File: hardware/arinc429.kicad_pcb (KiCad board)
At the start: 2 copper layers, 40 x 60 mm, 50 parts, among them P1 CON-SENSOR2, P2 BOOT, P3 DEBUG, P4 IND 8Pol, U1 XMC1404, U2 DRILL, U3 DRILL, U4 DRILL, U5 DRILL, U6 HI-3593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

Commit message: pcb design
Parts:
- moved RP6 43.6 mm to (109.0, 105.9), turned to 180 degrees
- moved D3 42.9 mm to (107.7, 102.6), turned to 270 degrees
- moved D9 41.1 mm to (109.1, 102.6), turned to 270 degrees
- moved D8 39.4 mm to (110.5, 102.6), turned to 270 degrees
- moved C6 21.0 mm to (124.0, 113.1), turned to 90 degrees
- moved P3 19.7 mm to (137.0, 109.2)
- moved C4 19.4 mm to (125.4, 113.1), turned to 90 degrees
- moved P2 17.6 mm to (137.0, 107.3), turned to 180 degrees
- moved C5 13.0 mm to (129.0, 119.3), turned to 270 degrees
- moved C3 11.0 mm to (135.1, 119.3), turned to 270 degrees
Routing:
- net VCC: track 11.5 -> 90.3 mm, vias 0 -> 2
- net GND: track 0.00 -> 29.6 mm
- net MB1-1: track 0.00 -> 25.4 mm, vias 0 -> 2
- net MB1-2: track 0.00 -> 24.3 mm, vias 0 -> 2
- net MB1-3: track 0.00 -> 23.1 mm, vias 0 -> 2
- net MB2-1: track 0.00 -> 22.3 mm, vias 0 -> 2
- net R1INT: track 0.00 -> 17.0 mm, vias 0 -> 2
- net R2FLAG: track 0.00 -> 16.8 mm, vias 0 -> 2
- net R2INT: track 0.00 -> 15.9 mm, vias 0 -> 2
- net R1FLAG: track 0.00 -> 15.7 mm, vias 0 -> 2
- net MB2-2: track 0.00 -> 15.5 mm, vias 0 -> 2
- net MB2-3: track 0.00 -> 15.5 mm, vias 0 -> 2
- net TFULL: track 0.00 -> 13.3 mm, vias 0 -> 2
- net TEMPY: track 0.00 -> 13.1 mm, vias 0 -> 2
- net Net-(C8-Pad1): track 0.00 -> 5.94 mm
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
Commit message: pcb prototyp
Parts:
- removed RP6: 1k, kicad-libraries:4X0402
- added G***: LOGO, kicad-libraries:Logo_TF_10x12, F.Cu at (109.0, 114.7)
- added R1: 1k, kicad-libraries:R0603F, F.Cu at (136.7, 145.4)
- added R10: 1k, kicad-libraries:R0603F, F.Cu at (103.4, 145.4)
- added R11: 1k, kicad-libraries:R0603F, F.Cu at (110.3, 102.0)
- moved D8 52.9 mm to (136.7, 148.5), turned to 90 degrees
- moved D9 46.3 mm to (103.4, 148.5), turned to 90 degrees
- moved C3 2.75 mm to (136.0, 116.7)
- moved P3 2.73 mm to (138.3, 106.8)
- moved C9 2.16 mm to (137.5, 109.1)
- moved X1 2.16 mm to (137.5, 111.8)
- moved C8 2.16 mm to (137.5, 114.5)
- moved P2 1.54 mm to (135.6, 106.7), turned to 270 degrees
- moved D3 1.34 mm to (108.9, 102.0), turned to 90 degrees
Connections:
- U1 pad 2: Net-(U1-Pad2) -> Status_LED
- U1 pad 21: CLOCK -> Net-(U1-Pad21)
- U1 pad 22: RESET -> Net-(U1-Pad22)
- U1 pad 33: Net-(RP6-Pad8) -> CLOCK
- U1 pad 34: Net-(RP6-Pad7) -> TX_LED
- U1 pad 36: Net-(U1-Pad36) -> RESET
- U1 pad 39: Net-(U1-Pad39) -> RX_LED
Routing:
- net VCC: track 90.3 -> 177.8 mm, vias 2 -> 4
- net RX_LED: track 0.00 -> 84.7 mm, vias 0 -> 2
- net GND: track 29.6 -> 89.8 mm, vias 0 -> 38
- net TX_LED: track 0.00 -> 30.5 mm, vias 0 -> 2
- net Status_LED: track 0.00 -> 28.0 mm
- net RESET: track 0.00 -> 25.5 mm
- net CLOCK: track 0.00 -> 24.5 mm
- net Net-(P3-Pad1): track 0.00 -> 6.67 mm
- net Net-(P2-Pad2): track 0.00 -> 3.74 mm
- net Net-(C8-Pad1): track 5.94 -> 8.21 mm
- net Net-(C9-Pad1): track 3.72 -> 5.87 mm
- net Net-(D9-Pad2): track 0.00 -> 1.50 mm
- net Net-(D8-Pad2): track 0.00 -> 1.50 mm
- net Net-(D3-Pad2): track 0.00 -> 1.44 mm
- net Net-(D6-Pad1): track 17.0 -> 16.2 mm
- added copper zone on F.Cu, net (none)
- added copper zone on F.Cu, net GND
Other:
- board text added: "Arinc 429 1.0"
- board text added: "Receive"
- board text added: "Status"
- board text added: "Transmit"

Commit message: ready for prototype
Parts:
- removed the G*** at (109.0, 114.7)
- added Fiducial_Mark: VAL**, kicad-libraries:Fiducial_Mark, F.Cu at (138.0, 153.0)
- added Fiducial_Mark: VAL**, kicad-libraries:Fiducial_Mark, F.Cu at (102.0, 142.0)
- added Fiducial_Mark: VAL**, kicad-libraries:Fiducial_Mark, F.Cu at (133.0, 103.0)
- added Fiducial_Mark: VAL**, kicad-libraries:Fiducial_Mark, F.Cu at (104.0, 109.0)
- added G***: LOGO, kicad-libraries:Logo_CoMCU, B.Cu at (120.0, 129.0)
- added G***: LOGO, kicad-libraries:Logo_31x31, F.Cu at (109.0, 114.2)
- added VAL: WEEE_7mm, kicad-libraries:WEEE_7mm, B.Cu at (112.3, 129.5)
- added VAL: CE_5mm, kicad-libraries:CE_5mm, B.Cu at (128.0, 129.0)
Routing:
- net GND: track 89.8 -> 91.9 mm, vias 38 -> 44
- net Net-(C13-Pad1): track 3.22 -> 4.21 mm
- net R2FLAG: track 16.8 -> 16.2 mm
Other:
- board text added: "A"
- board text added: "ARINC 429 1.0"
- board text added: "B"
- board text added: "GND"
- board text added: "RX1"
- board text added: "RX1AIN"
- board text added: "RX1BIN"
- board text added: "RX2"
- board text added: "RX2AIN"
- board text added: "RX2BIN"
- board text added: "TX"
- board text added: "TXAOUT"
- board text added: "TXBOUT"
- board text added: "tinkerforge.com"
- board text removed: "Arinc 429 1.0"

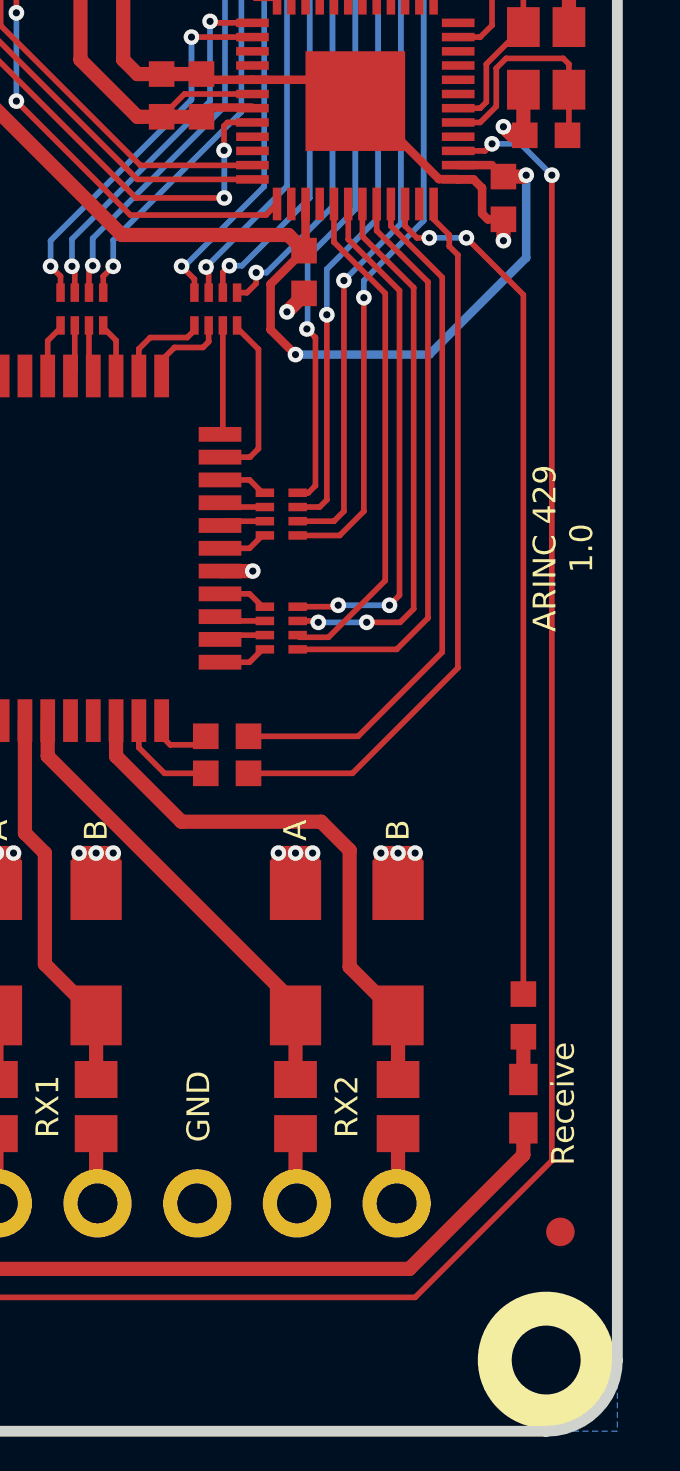
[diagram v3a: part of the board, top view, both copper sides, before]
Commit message: fixed copper floodfill
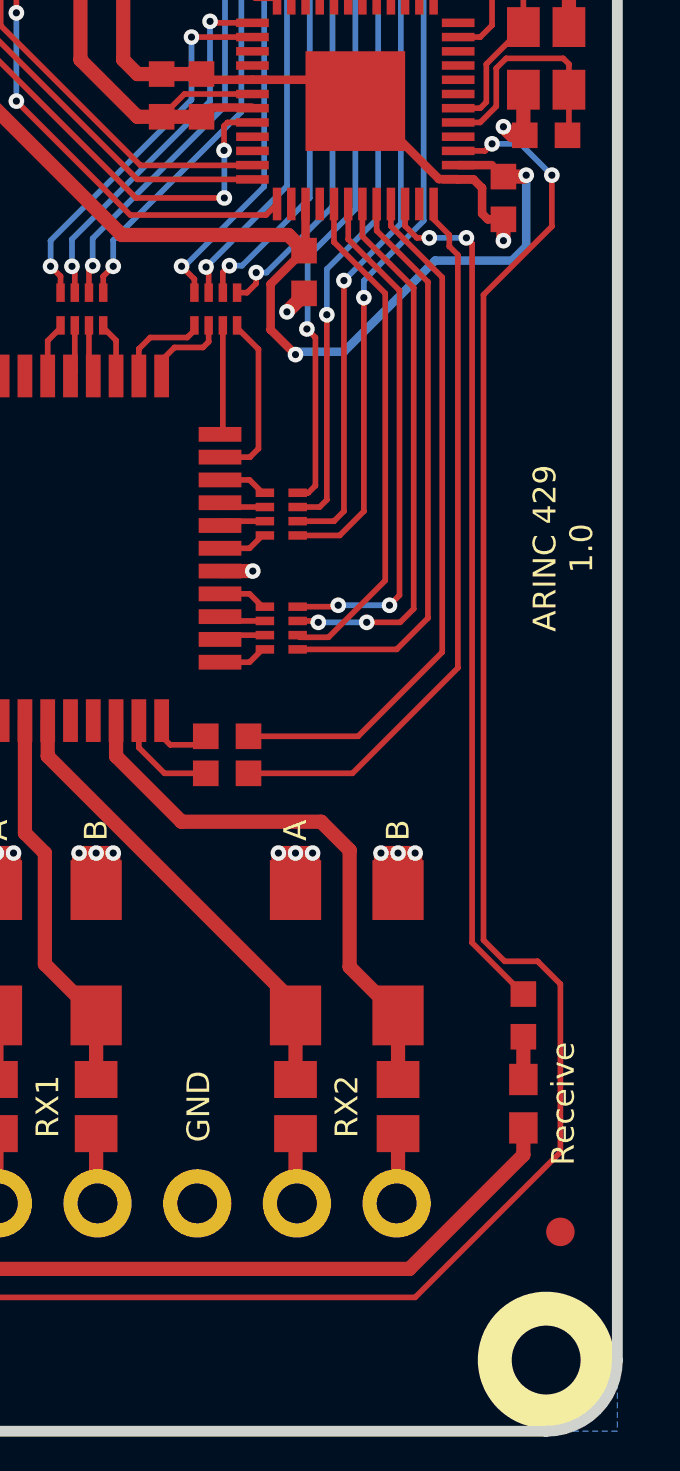
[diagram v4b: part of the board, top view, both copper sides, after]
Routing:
- net RX_LED: track 84.7 -> 87.7 mm
- removed copper zone on F.Cu, net (none)

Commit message: add description text on top side
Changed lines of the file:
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@@
-(kicad_pcb (version 20171130) (host pcbnew 5.1.6-c6e7f7d~86~ubuntu20.04.1)
+(kicad_pcb (version 20171130) (host pcbnew 5.1.6-c6e7f7d~86~ubuntu18.04.1)
   (general
     (thickness 1.6)
-    (drawings 33)
+    (drawings 39)
     (tracks 610)
     (zones 0)
@@
   (layers
     (0 F.Cu signal)
-    (31 B.Cu signal)
+    (31 B.Cu signal hide)
     (32 B.Adhes user)
     (33 F.Adhes user)
@@
       (psnegative false)
       (psa4output false)
-      (plotreference true)
-      (plotvalue true)
+      (plotreference false)
+      (plotvalue false)
       (plotinvisibletext false)
       (padsonsilk false)
-      (subtractmaskfromsilk false)
+      (subtractmaskfromsilk true)
       (outputformat 1)
       (mirror false)
       (drillshape 0)
       (scaleselection 1)
-      (outputdirectory "../../../Schreibtisch/proto/arinc429/"))
+      (outputdirectory "pcb/"))
   )
   (net 0 "")
@@
     )
   )
+  (gr_text B (at 133.8 149.95 90) (layer F.SilkS)
+    (effects (font (size 0.8 0.8) (thickness 0.15)))
+  )
+  (gr_text A (at 127.25 149.95 90) (layer F.SilkS)
+    (effects (font (size 0.8 0.8) (thickness 0.15)))
+  )
+  (gr_text B (at 123.25 149.95 90) (layer F.SilkS)
+    (effects (font (size 0.8 0.8) (thickness 0.15)))
+  )
+  (gr_text A (at 116.75 149.95 90) (layer F.SilkS)
+    (effects (font (size 0.8 0.8) (thickness 0.15)))
+  )
+  (gr_text A (at 106.15 149.95 90) (layer F.SilkS)
+    (effects (font (size 0.8 0.8) (thickness 0.15)))
+  )
+  (gr_text B (at 112.95 149.95 90) (layer F.SilkS)
+    (effects (font (size 0.8 0.8) (thickness 0.15)))
+  )
   (gr_text GND (at 125.3 148.6 90) (layer F.SilkS)

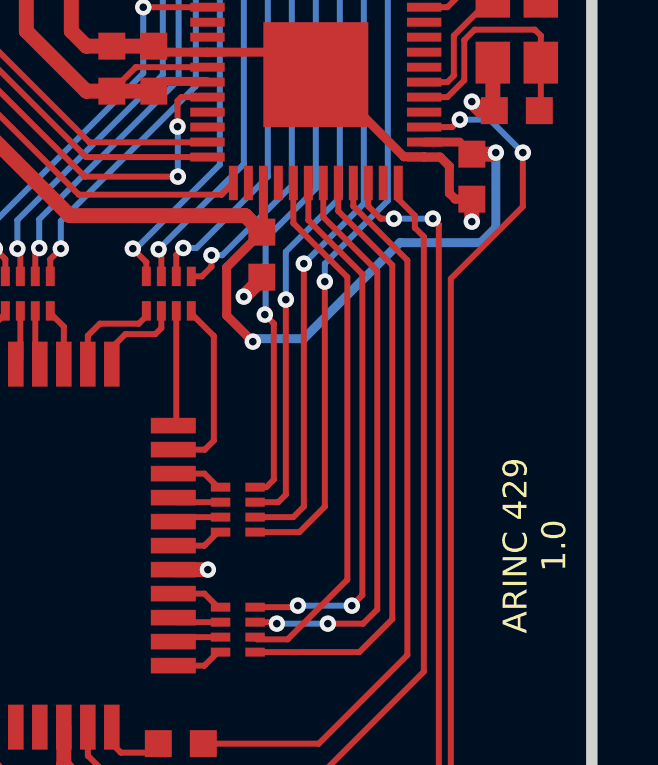
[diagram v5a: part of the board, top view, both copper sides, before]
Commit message: changed spi pinout
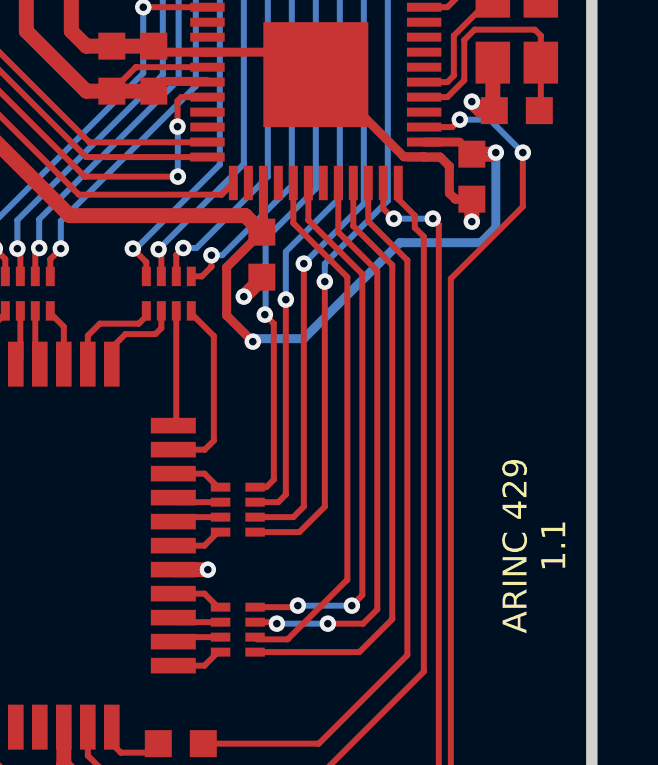
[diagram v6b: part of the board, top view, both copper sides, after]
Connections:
- U1 pad 31: M-CLK -> Net-(U1-Pad31)
- U1 pad 32: M-CS -> M-CLK
- U1 pad 33: CLOCK -> M-CS
- U1 pad 34: TX_LED -> CLOCK
- U1 pad 35: Net-(U1-Pad35) -> TX_LED
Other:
- board text added: "ARINC 429 1.1"
- board text removed: "ARINC 429 1.0"
